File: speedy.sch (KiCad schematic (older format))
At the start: 40 parts, among them U1 STM32F415RGT6, U2 NUF2042VX6, X1 16Mhz 10ppm

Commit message: Regenerate netlist & Start placing footprints
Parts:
- removed W1, W2: TEST, _std:Measurement_Point_Round-SMD-Pad_Small, symbol TEST
- CONN1: footprint MODULE -> _connectors:_Molex-PicoBlade-SMD-8
- D1, D2, D3, D4: footprint LEDs:LED-0603 -> _std:_LED_0603
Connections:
- net I2C1_SCL: now also R6.2, U1.58 (PB6)
- net I2C1_SDA: now also R8.2, U1.59 (PB7)
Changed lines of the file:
@@
 EESchema Schematic File Version 2
-LIBS:speedy-rescue
 LIBS:speedy-cache
 LIBS:power
@@
 $EndDescr
 $Comp
-L VCC #PWR1
+L VCC #PWR01
 U 1 1 5537E86E
 P 1325 2325
-F 0 "#PWR1" H 1325 2175 50  0001 C CNN
+F 0 "#PWR01" H 1325 2175 50  0001 C CNN
 F 1 "VCC" H 1325 2475 50  0000 C CNN
 F 2 "" H 1325 2325 60  0000 C CNN
@@
 $EndComp
 $Comp
-L GND #PWR2
+L GND #PWR02
 U 1 1 5537E888
 P 1325 2675
-F 0 "#PWR2" H 1325 2425 50  0001 C CNN
+F 0 "#PWR02" H 1325 2425 50  0001 C CNN
 F 1 "GND" H 1325 2525 50  0000 C CNN
 F 2 "" H 1325 2675 60  0000 C CNN
@@
 $EndComp
 $Comp
-L VCC #PWR3
+L VCC #PWR03
 U 1 1 55380A17
 P 1650 1200
-F 0 "#PWR3" H 1650 1050 50  0001 C CNN
+F 0 "#PWR03" H 1650 1050 50  0001 C CNN
 F 1 "VCC" H 1650 1350 50  0000 C CNN
 F 2 "" H 1650 1200 60  0000 C CNN
@@
 $EndComp
 $Comp
-L GND #PWR4
+L GND #PWR04
 U 1 1 55380A35
 P 1650 1850
-F 0 "#PWR4" H 1650 1600 50  0001 C CNN
+F 0 "#PWR04" H 1650 1600 50  0001 C CNN
 F 1 "GND" H 1650 1700 50  0000 C CNN
 F 2 "" H 1650 1850 60  0000 C CNN
@@
 STM32F4_NRST
 $Comp
-L GND #PWR7
+L GND #PWR05
 U 1 1 55367951
 P 1875 3250
-F 0 "#PWR7" H 1875 3000 50  0001 C CNN
+F 0 "#PWR05" H 1875 3000 50  0001 C CNN
 F 1 "GND" H 1875 3100 50  0000 C CNN
 F 2 "" H 1875 3250 60  0000 C CNN
@@
 $EndComp
 $Comp
-L GND #PWR6
+L GND #PWR06
 U 1 1 55367998
 P 1875 3050
-F 0 "#PWR6" H 1875 2800 50  0001 C CNN
+F 0 "#PWR06" H 1875 2800 50  0001 C CNN
 F 1 "GND" H 1875 2900 50  0000 C CNN
 F 2 "" H 1875 3050 60  0000 C CNN
@@
 $EndComp
 $Comp
-L GND #PWR5
+L GND #PWR07
 U 1 1 553688C7
 P 1750 3850
-F 0 "#PWR5" H 1750 3600 50  0001 C CNN
+F 0 "#PWR07" H 1750 3600 50  0001 C CNN
 F 1 "GND" H 1750 3700 50  0000 C CNN
 F 2 "" H 1750 3850 60  0000 C CNN
@@
 $EndComp
 $Comp
-L GND #PWR8
+L GND #PWR08
 U 1 1 55369B95
 P 1950 1850
-F 0 "#PWR8" H 1950 1600 50  0001 C CNN
+F 0 "#PWR08" H 1950 1600 50  0001 C CNN
 F 1 "GND" H 1950 1700 50  0000 C CNN
 F 2 "" H 1950 1850 60  0000 C CNN
@@
 $EndComp
 $Comp
-L GND #PWR11
+L GND #PWR09
 U 1 1 553697B0
 P 4775 7450
-F 0 "#PWR11" H 4775 7200 50  0001 C CNN
+F 0 "#PWR09" H 4775 7200 50  0001 C CNN
 F 1 "GND" H 4775 7300 50  0000 C CNN
 F 2 "" H 4775 7450 60  0000 C CNN
@@
 Text Label 3875 2250 0    39   ~ 0
 SPI1_MOSI
-Text Label 5525 3850 0    39   ~ 0
+Text Label 5125 3850 0    39   ~ 0
 I2C1_SCL
-Text Label 5525 3950 0    39   ~ 0
+Text Label 5125 3950 0    39   ~ 0
 I2C1_SDA
 $Comp
@@
 NoConn ~ 8025 1700
 $Comp
-L GND #PWR15
+L GND #PWR010
 U 1 1 5537C35C
 P 6300 1300
-F 0 "#PWR15" H 6300 1050 50  0001 C CNN
+F 0 "#PWR010" H 6300 1050 50  0001 C CNN
 F 1 "GND" H 6300 1150 50  0000 C CNN
 F 2 "" H 6300 1300 60  0000 C CNN
@@
 SDIO_CMD
 $Comp
-L GND #PWR16
+L GND #PWR011
 U 1 1 553889C2
 P 6605 3050
-F 0 "#PWR16" H 6605 2800 50  0001 C CNN
+F 0 "#PWR011" H 6605 2800 50  0001 C CNN
 F 1 "GND" H 6605 2900 50  0000 C CNN
 F 2 "" H 6605 3050 60  0000 C CNN
@@
 SD_DETECT
 $Comp
-L GND #PWR25
+L GND #PWR012
 U 1 1 553898C6
 P 8280 3550
-F 0 "#PWR25" H 8280 3300 50  0001 C CNN
+F 0 "#PWR012" H 8280 3300 50  0001 C CNN
 F 1 "GND" H 8280 3400 50  0000 C CNN
 F 2 "" H 8280 3550 60  0000 C CNN
@@
 $EndComp
 $Comp
-L VCC #PWR9
+L VCC #PWR013
 U 1 1 5538C13D
 P 4575 5350
-F 0 "#PWR9" H 4575 5200 50  0001 C CNN
+F 0 "#PWR013" H 4575 5200 50  0001 C CNN
 F 1 "VCC" H 4575 5500 50  0000 C CNN
 F 2 "" H 4575 5350 60  0000 C CNN
@@
 $EndComp
 $Comp
-L VCC #PWR10
+L VCC #PWR014
 U 1 1 5538C1A8
 P 4725 5350
-F 0 "#PWR10" H 4725 5200 50  0001 C CNN
+F 0 "#PWR014" H 4725 5200 50  0001 C CNN
 F 1 "VCC" H 4725 5500 50  0000 C CNN
 F 2 "" H 4725 5350 60  0000 C CNN
@@
 $EndComp
 $Comp
-L VCC #PWR12
+L VCC #PWR015
 U 1 1 5538C213
 P 4875 5350
-F 0 "#PWR12" H 4875 5200 50  0001 C CNN
+F 0 "#PWR015" H 4875 5200 50  0001 C CNN
 F 1 "VCC" H 4875 5500 50  0000 C CNN
 F 2 "" H 4875 5350 60  0000 C CNN
@@
 $EndComp
 $Comp
-L VCC #PWR13
+L VCC #PWR016
 U 1 1 5538C27E
 P 5025 5350
-F 0 "#PWR13" H 5025 5200 50  0001 C CNN
+F 0 "#PWR016" H 5025 5200 50  0001 C CNN
 F 1 "VCC" H 5025 5500 50  0000 C CNN
 F 2 "" H 5025 5350 60  0000 C CNN
@@
 $EndComp
 $Comp
-L VCC #PWR14
+L VCC #PWR017
 U 1 1 5538C2E9
 P 5175 5350
-F 0 "#PWR14" H 5175 5200 50  0001 C CNN
+F 0 "#PWR017" H 5175 5200 50  0001 C CNN
 F 1 "VCC" H 5175 5500 50  0000 C CNN
 F 2 "" H 5175 5350 60  0000 C CNN
@@
 $EndComp
 $Comp
-L GND #PWR24
+L GND #PWR018
 U 1 1 55441855
 P 7900 1600
-F 0 "#PWR24" H 7900 1350 50  0001 C CNN
+F 0 "#PWR018" H 7900 1350 50  0001 C CNN
 F 1 "GND" H 7900 1450 50  0000 C CNN
 F 2 "" H 7900 1600 60  0000 C CNN
@@
 F 0 "D1" H 7590 5500 50  0000 C CNN
 F 1 "POWER" H 7590 5300 50  0000 C CNN
-F 2 "LEDs:LED-0603" H 7590 5400 60  0001 C CNN
+F 2 "_std:_LED_0603" H 7590 5400 60  0001 C CNN
 F 3 "" H 7590 5400 60  0000 C CNN
 	1    7590 5400
@@
 $EndComp
 $Comp
-L GND #PWR20
+L GND #PWR019
 U 1 1 55486437
 P 7890 5400
-F 0 "#PWR20" H 7890 5150 50  0001 C CNN
+F 0 "#PWR019" H 7890 5150 50  0001 C CNN
 F 1 "GND" H 7890 5250 50  0000 C CNN
 F 2 "" H 7890 5400 60  0000 C CNN
@@
 F 0 "D2" H 7590 5800 50  0000 C CNN
 F 1 "ERROR" H 7590 5600 50  0000 C CNN
-F 2 "LEDs:LED-0603" H 7590 5700 60  0001 C CNN
+F 2 "_std:_LED_0603" H 7590 5700 60  0001 C CNN
 F 3 "" H 7590 5700 60  0000 C CNN
 	1    7590 5700
@@
 $EndComp
 $Comp
-L GND #PWR21
+L GND #PWR020
 U 1 1 55486799
 P 7890 5700
-F 0 "#PWR21" H 7890 5450 50  0001 C CNN
+F 0 "#PWR020" H 7890 5450 50  0001 C CNN
 F 1 "GND" H 7890 5550 50  0000 C CNN
 F 2 "" H 7890 5700 60  0000 C CNN
@@
 F 0 "D3" H 7590 6100 50  0000 C CNN
 F 1 "STATUS" H 7590 5900 50  0000 C CNN
-F 2 "LEDs:LED-0603" H 7590 6000 60  0001 C CNN
+F 2 "_std:_LED_0603" H 7590 6000 60  0001 C CNN
 F 3 "" H 7590 6000 60  0000 C CNN
 	1    7590 6000
@@
 $EndComp
 $Comp
-L GND #PWR22
+L GND #PWR021
 U 1 1 5548696F
 P 7890 6000
-F 0 "#PWR22" H 7890 5750 50  0001 C CNN
+F 0 "#PWR021" H 7890 5750 50  0001 C CNN
 F 1 "GND" H 7890 5850 50  0000 C CNN
 F 2 "" H 7890 6000 60  0000 C CNN
@@
 F 0 "D4" H 7590 6400 50  0000 C CNN
 F 1 "HEARTBEAT" H 7590 6200 50  0000 C CNN
-F 2 "LEDs:LED-0603" H 7590 6300 60  0001 C CNN
+F 2 "_std:_LED_0603" H 7590 6300 60  0001 C CNN
 F 3 "" H 7590 6300 60  0000 C CNN
 	1    7590 6300
@@
 $EndComp
 $Comp
-L GND #PWR23
+L GND #PWR022
 U 1 1 55486983
 P 7890 6300
-F 0 "#PWR23" H 7890 6050 50  0001 C CNN
+F 0 "#PWR022" H 7890 6050 50  0001 C CNN
 F 1 "GND" H 7890 6150 50  0000 C CNN
 F 2 "" H 7890 6300 60  0000 C CNN
@@
 $EndComp
 $Comp
-L VCC #PWR17
+L VCC #PWR023
 U 1 1 55486C47
 P 6915 5400
-F 0 "#PWR17" H 6915 5250 50  0001 C CNN
+F 0 "#PWR023" H 6915 5250 50  0001 C CNN
 F 1 "VCC" H 6915 5550 50  0000 C CNN
 F 2 "" H 6915 5400 60  0000 C CNN
@@
 Text Notes 6100 5325 0    60   ~ 0
 LEDs
-$Comp
-L TEST W1
-U 1 1 5577C23F
-P 5075 3850
-F 0 "W1" H 5225 3875 28  0000 C CNN
-F 1 "TEST" H 5075 3850 20  0000 C CNN
-F 2 "_std:Measurement_Point_Round-SMD-Pad_Small" H 5075 3850 60  0001 C CNN
-F 3 "" H 5075 3850 60  0000 C CNN
-	1    5075 3850
-	1    0    0    -1
-$EndComp
-$Comp
-L TEST W2
-U 1 1 5577DD1D
-P 5150 3950
-F 0 "W2" H 5300 3975 28  0000 C CNN
-F 1 "TEST" H 5150 3950 20  0000 C CNN
-F 2 "_std:Measurement_Point_Round-SMD-Pad_Small" H 5150 3950 60  0001 C CNN
-F 3 "" H 5150 3950 60  0000 C CNN
-	1    5150 3950
-	1    0    0    -1
-$EndComp
 Text GLabel 4875 3375 2    39   Input ~ 0
 VCCA
@@
 	4600 3775 4600 3850
 Wire Wire Line
-	3825 3850 4875 3850
-Wire Wire Line
-	3825 3950 4950 3950
+	3825 3850 5125 3850
+Wire Wire Line
+	3825 3950 5125 3950
 Connection ~ 4250 7450
 Wire Wire Line
@@
 	6000 2150 8870 2150
 Wire Wire Line
-	5275 3850 5525 3850
-Wire Wire Line
-	5350 3950 5525 3950
-Wire Wire Line
 	3875 3550 3825 3550
 Wire Wire Line
@@
 F 0 "CONN1" H 7950 5050 50  0000 C CNN
 F 1 "JTAG" H 7950 4050 50  0000 C CNN
-F 2 "MODULE" H 7950 4550 50  0001 C CNN
+F 2 "_connectors:_Molex-PicoBlade-SMD-8" H 7950 4550 50  0001 C CNN
 F 3 "DOCUMENTATION" H 7950 4550 50  0001 C CNN
 	1    7950 4550
@@
 $EndComp
 $Comp
-L GND #PWR19
+L GND #PWR024
 U 1 1 55C9683C
 P 7575 4300
-F 0 "#PWR19" H 7575 4050 50  0001 C CNN
+F 0 "#PWR024" H 7575 4050 50  0001 C CNN
 F 1 "GND" H 7575 4150 50  0000 C CNN
 F 2 "" H 7575 4300 60  0000 C CNN
@@
 	7575 4300 7600 4300
 $Comp
-L VCC #PWR18
+L VCC #PWR025
 U 1 1 55C96AB4
 P 7525 4175
-F 0 "#PWR18" H 7525 4025 50  0001 C CNN
+F 0 "#PWR025" H 7525 4025 50  0001 C CNN
 F 1 "VCC" H 7525 4325 50  0000 C CNN
 F 2 "" H 7525 4175 60  0000 C CNN

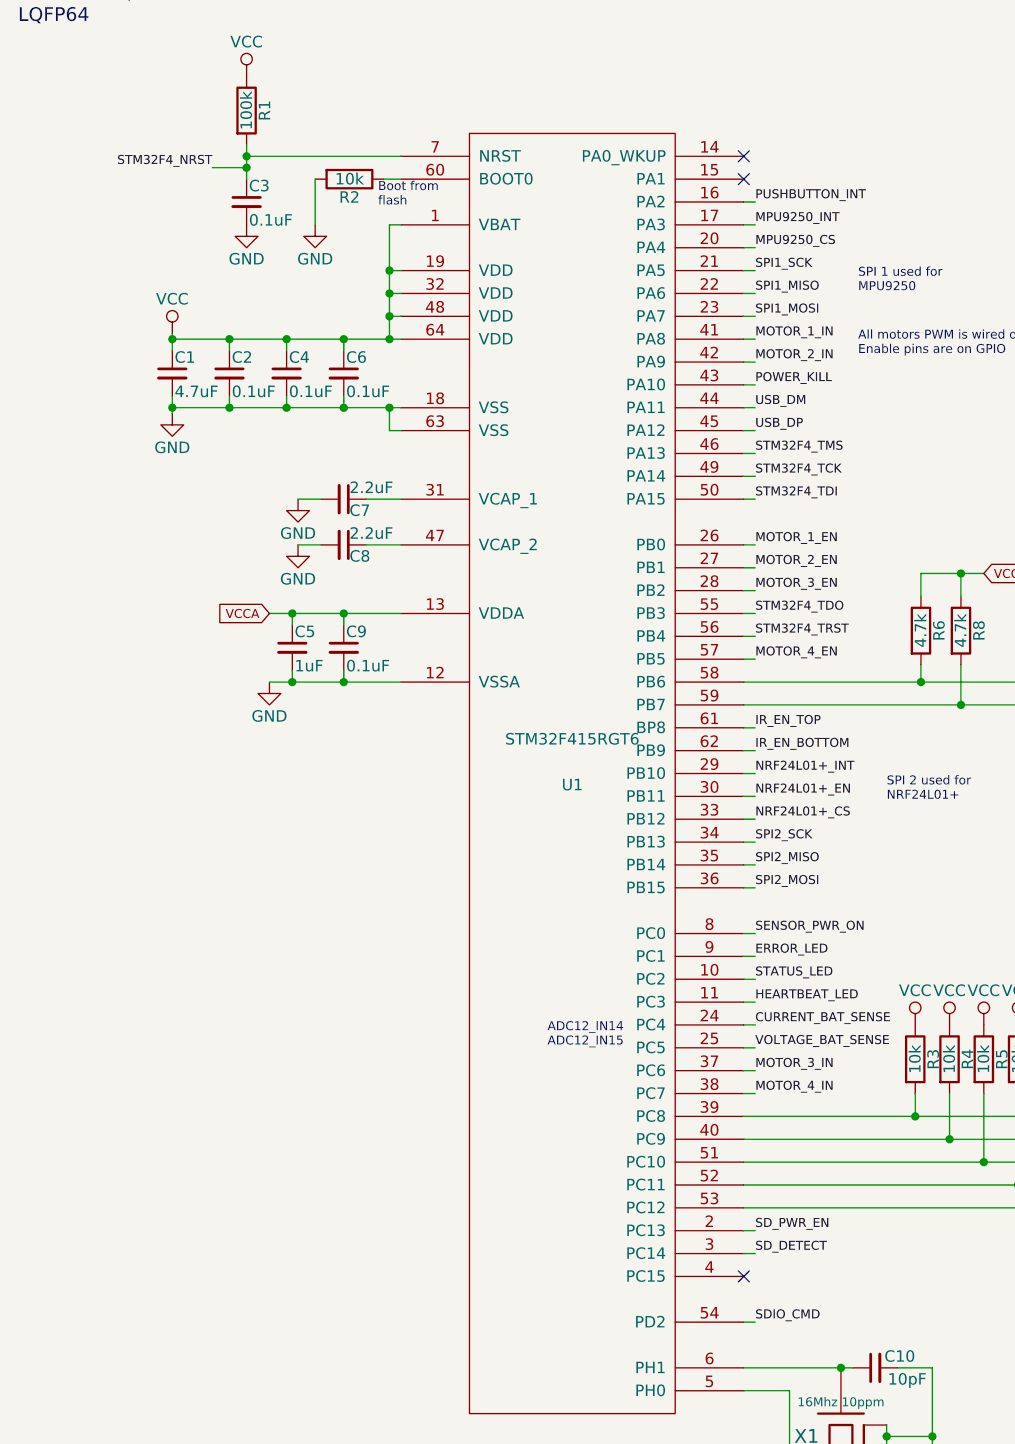
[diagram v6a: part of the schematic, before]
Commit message: Finish placing components on PCB
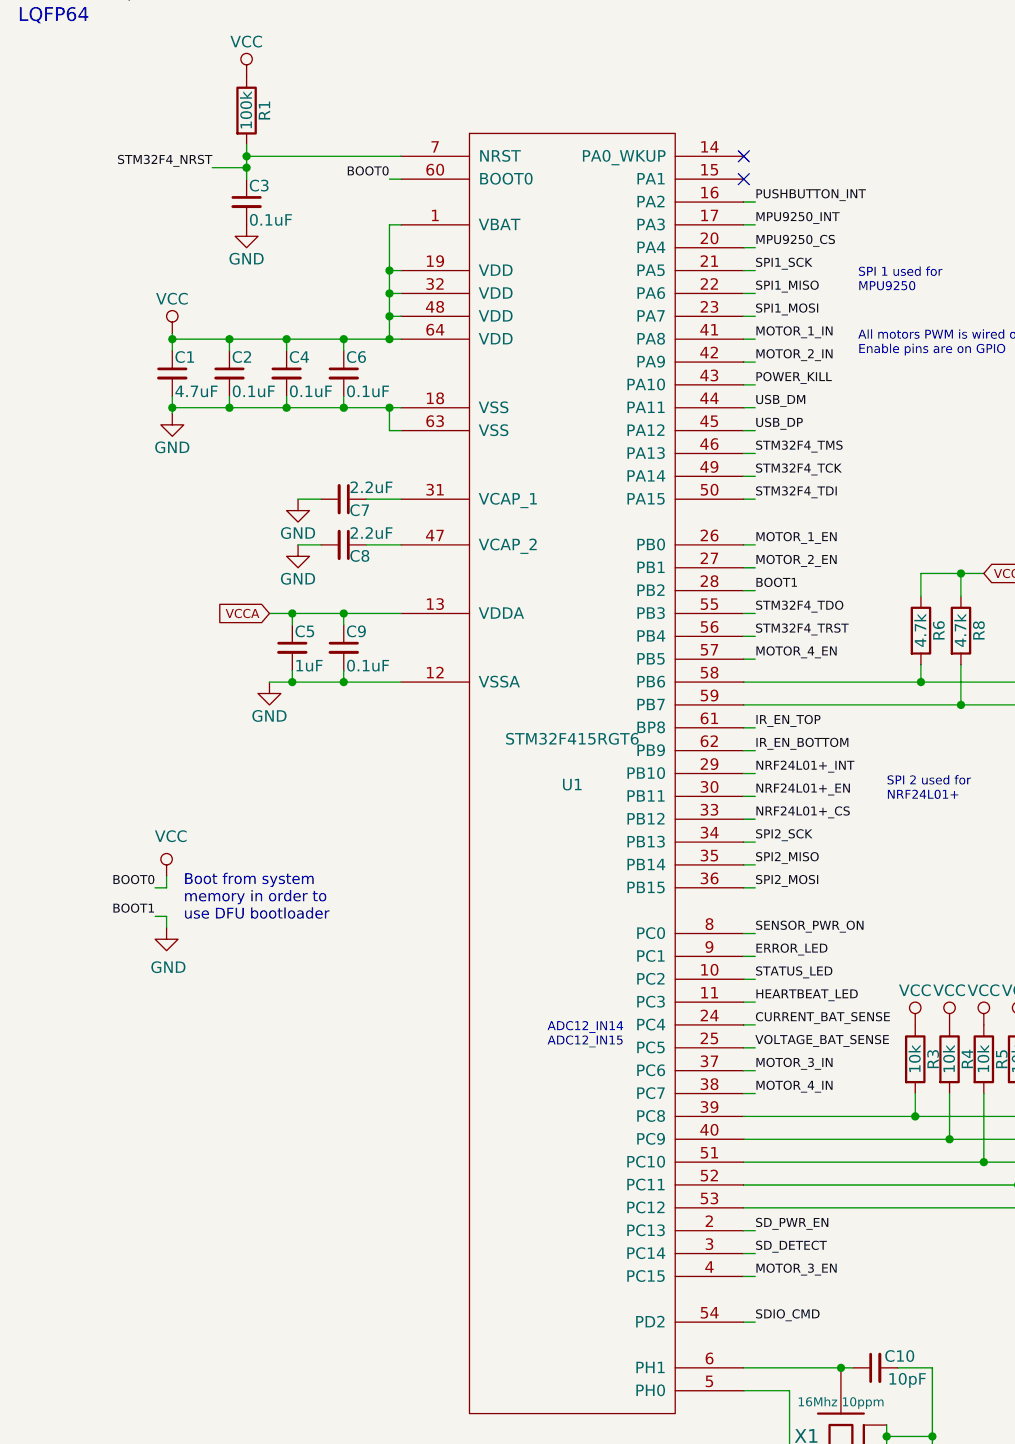
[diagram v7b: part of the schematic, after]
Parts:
- removed R2: 10k, _std:_0402, symbol R
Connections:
- net GND: now also U1.28 (PB2)
- net MOTOR_3_EN: now also U1.4 (PC15); no longer U1.28 (PB2)
- net VCC: now also U1.60 (BOOT0)
- no-connect marks 5 -> 4
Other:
- note added: "Boot from system\nmemory in order to \nuse DFU bootloader"
- note removed: "Boot from\nflash"
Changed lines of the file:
@@
-$EndComp
-$Comp
-L R R2
-U 1 1 55369A15
-P 2100 1650
-F 0 "R2" V 2180 1650 50  0000 C CNN
-F 1 "10k" V 2100 1650 50  0000 C CNN
-F 2 "_std:_0402" V 2030 1650 30  0001 C CNN
-F 3 "" H 2100 1650 30  0000 C CNN
-	1    2100 1650
-	0    1    1    0
-$EndComp
-$Comp
-L GND #PWR08
-U 1 1 55369B95
-P 1950 1850
-F 0 "#PWR08" H 1950 1600 50  0001 C CNN
-F 1 "GND" H 1950 1700 50  0000 C CNN
-F 2 "" H 1950 1850 60  0000 C CNN
-F 3 "" H 1950 1850 60  0000 C CNN
-	1    1950 1850
-	1    0    0    -1
 $EndComp
 $Comp
@@
 Text Label 3875 3350 0    39   ~ 0
 MOTOR_2_EN
-Text Label 3875 3450 0    39   ~ 0
+Text Label 3875 6450 0    39   ~ 0
 MOTOR_3_EN
 Text Label 3875 3750 0    39   ~ 0
@@
 Text Label 3875 2950 0    39   ~ 0
 STM32F4_TCK
-Text Notes 2225 1775 0    39   ~ 0
-Boot from\nflash
 $Comp
 L LED-RESCUE-speedy D1
@@
 	0    -1   -1   0
 $EndComp
-NoConn ~ 3825 6450
 NoConn ~ 3825 1650
 NoConn ~ 3825 1550
@@
 Wire Wire Line
 	3825 6850 4300 6850
-Wire Wire Line
-	1950 1650 1950 1850
 Connection ~ 1650 1600
 Wire Wire Line
@@
 Connection ~ 4775 3375
 Wire Wire Line
-	2250 1650 2325 1650
+	2275 1650 2325 1650
 Wire Wire Line
 	2325 1850 2275 1850
@@
 Wire Wire Line
 	3875 3350 3825 3350
-Wire Wire Line
-	3825 3450 3875 3450
 Wire Wire Line
 	3875 5650 3825 5650
@@
 Wire Wire Line
 	7525 4200 7600 4200
+Wire Wire Line
+	3875 6450 3825 6450
+Text Label 3875 3450 0    39   ~ 0
+BOOT1
+Wire Wire Line
+	3875 3450 3825 3450
+Text Label 2275 1650 2    39   ~ 0
+BOOT0
+Text Label 1250 4750 2    39   ~ 0
+BOOT0
+Text Label 1250 4875 2    39   ~ 0
+BOOT1
+$Comp
+L GND #PWR?
+U 1 1 56A0A41F
+P 1300 4925
+F 0 "#PWR?" H 1300 4675 50  0001 C CNN
+F 1 "GND" H 1308 4751 50  0000 C CNN
+F 2 "" H 1300 4925 60  0000 C CNN
+F 3 "" H 1300 4925 60  0000 C CNN
+	1    1300 4925
+	1    0    0    -1
+$EndComp
+Wire Wire Line
+	1300 4925 1300 4875
+Wire Wire Line
+	1300 4875 1250 4875
+$Comp
+L VCC #PWR?
+U 1 1 56A0A6B3
+P 1300 4700
+F 0 "#PWR?" H 1300 4550 50  0001 C CNN
+F 1 "VCC" H 1320 4874 50  0000 C CNN
+F 2 "" H 1300 4700 60  0000 C CNN
+F 3 "" H 1300 4700 60  0000 C CNN
+	1    1300 4700
+	1    0    0    -1
+$EndComp
+Wire Wire Line
+	1300 4700 1300 4750
+Wire Wire Line
+	1300 4750 1250 4750
+Text Notes 1375 4900 0    47   ~ 0
+Boot from system\nmemory in order to \nuse DFU bootloader
 $EndSCHEMATC
